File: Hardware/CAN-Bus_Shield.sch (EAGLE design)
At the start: 38 parts, among them Q1 16MHz, U1 USD-SOCKETNEW, U2 ARDUINO_SHIELDLABEL, U3 EM406, U4 MCP2515, U5 MCP2551, U6 HEX_CONVERTER, U7 JOYSTICK_MINI4UCON, X1 DB9 Plug

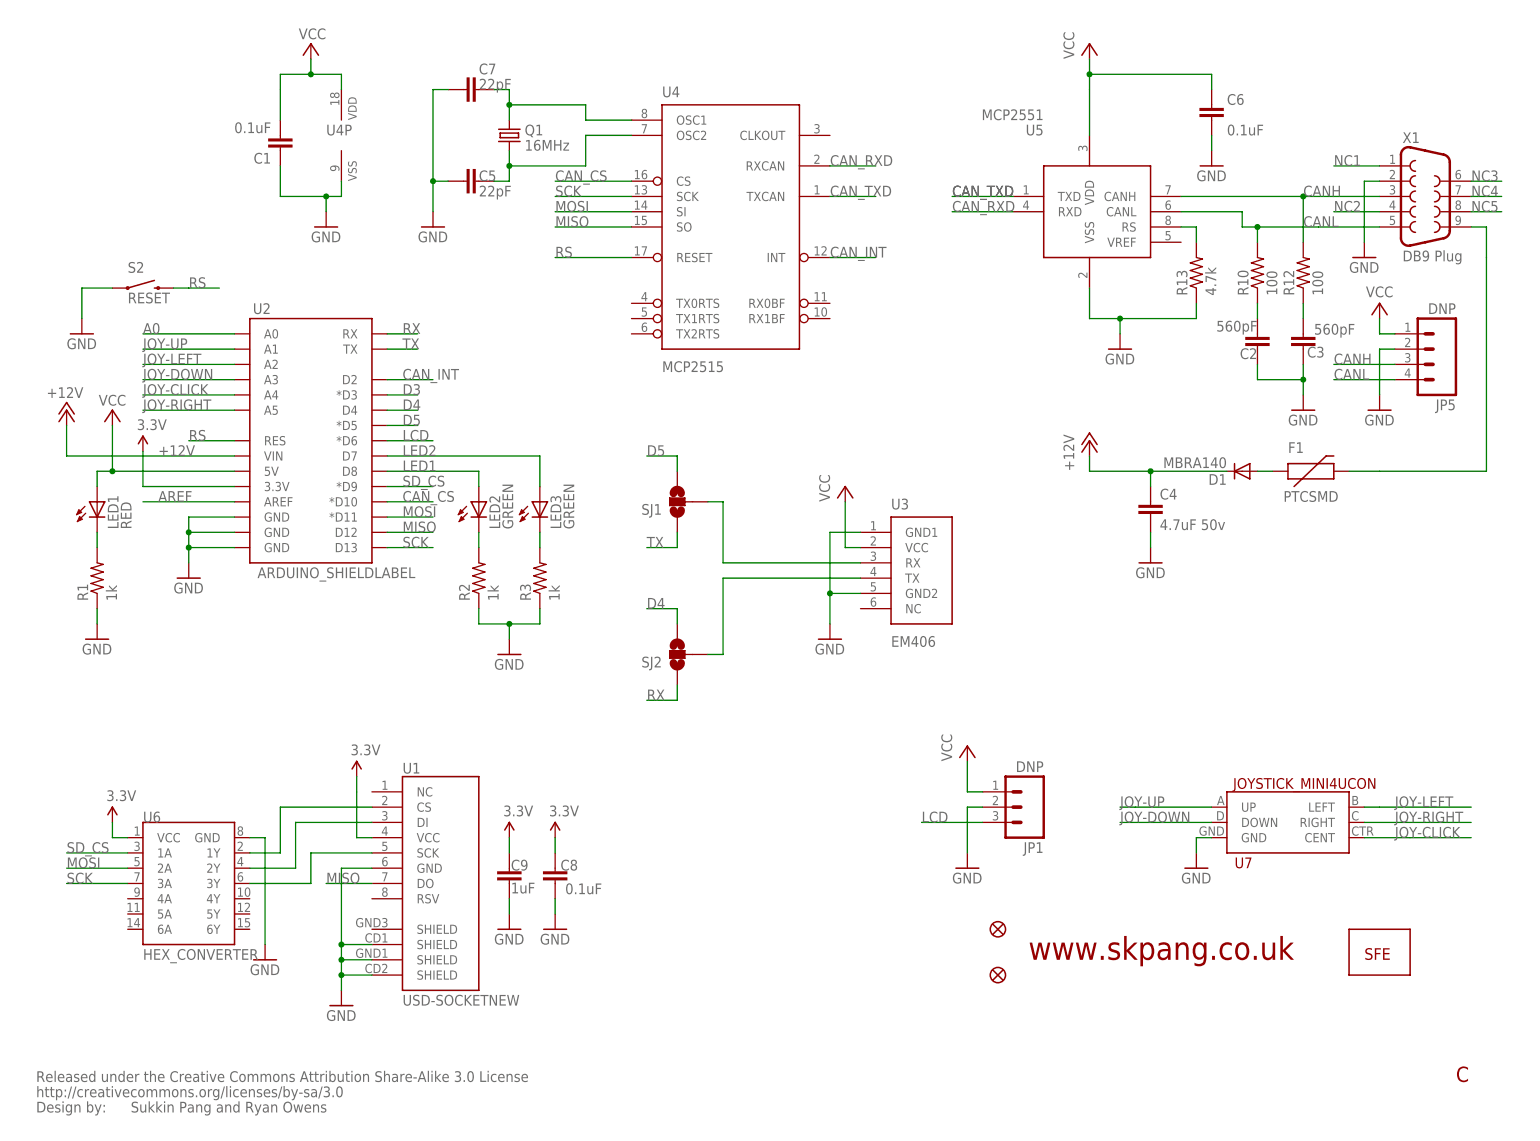
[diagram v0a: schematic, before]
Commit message: Updating Board files to R3/Leonardo layout
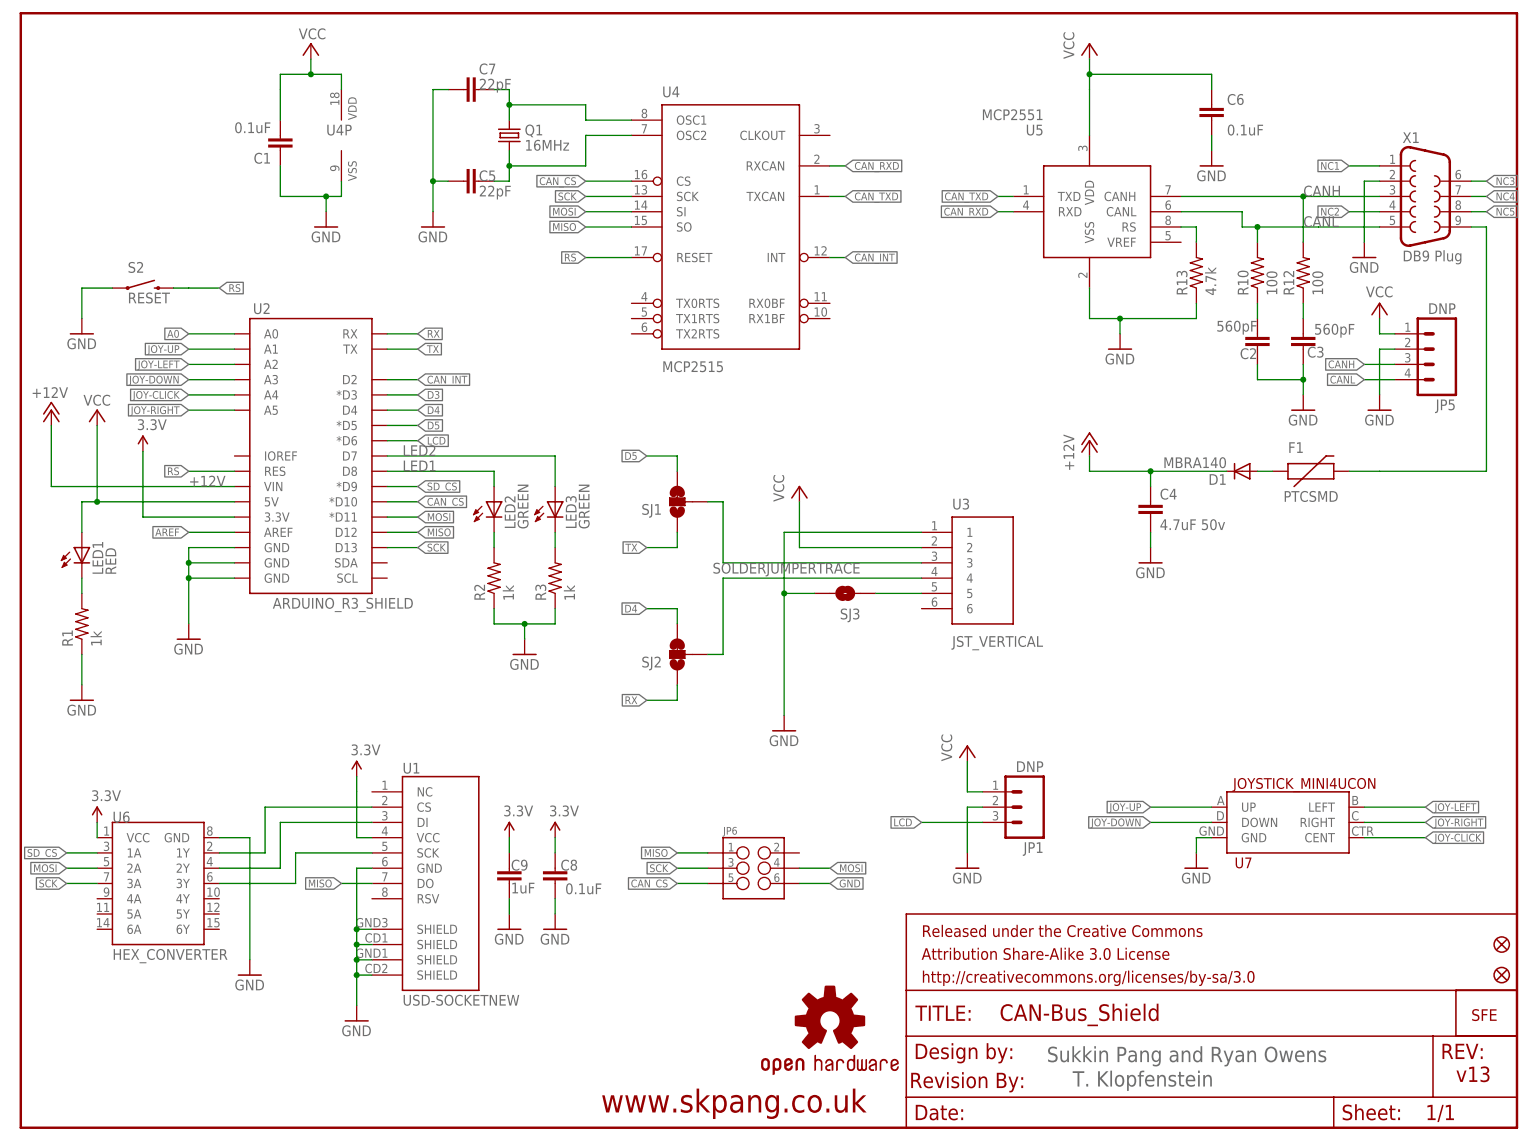
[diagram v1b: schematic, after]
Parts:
- added FRAME1: FRAME-LETTER, SparkFun-Aesthetics:FRAME-LETTER
- added JP6: (no value), SparkFun-Connectors:M03X2NO_SILK
- added LOGO1: OSHW-LOGOM, SparkFun-Aesthetics:OSHW-LOGOM
- added SJ3: SOLDERJUMPERTRACE, SparkFun-Passives:SOLDERJUMPERTRACE
- U$1: value CREATIVE_COMMONS -> REVISION; device SparkFun:CREATIVE_COMMONS -> SparkFun-Aesthetics:REVISION
- U2: value ARDUINO_SHIELDLABEL -> ARDUINO_R3_SHIELD; device SparkFun:ARDUINO_SHIELDLABEL -> SparkFun-Boards:ARDUINO_R3_SHIELD
- U3: value EM406 -> JST_VERTICAL; device SparkFun:EM406 -> SparkFun-Connectors:JST_VERTICAL
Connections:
- new net N$1: SJ3.1, U3.5
- net CAN_CS: now also JP6.5
- net GND: now also JP6.6, SJ3.2, U1.SHIELD@1, U3.1; no longer U3.GND1, U3.GND2
- net MISO: now also JP6.1
- net MOSI: now also JP6.4
- net N$21: now also U3.3; no longer U3.RX
- net N$22: now also U3.4; no longer U3.TX
- net SCK: now also JP6.3
- net VCC: now also U3.2; no longer U3.VCC
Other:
- note added: "T. Klopfenstein"
- note added: "v13"
- note removed: "C"
- moved on the sheet: LED1, LED2, LED3, R1, R2, R3, U3, U6
